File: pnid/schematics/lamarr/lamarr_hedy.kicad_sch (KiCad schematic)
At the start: 98 parts

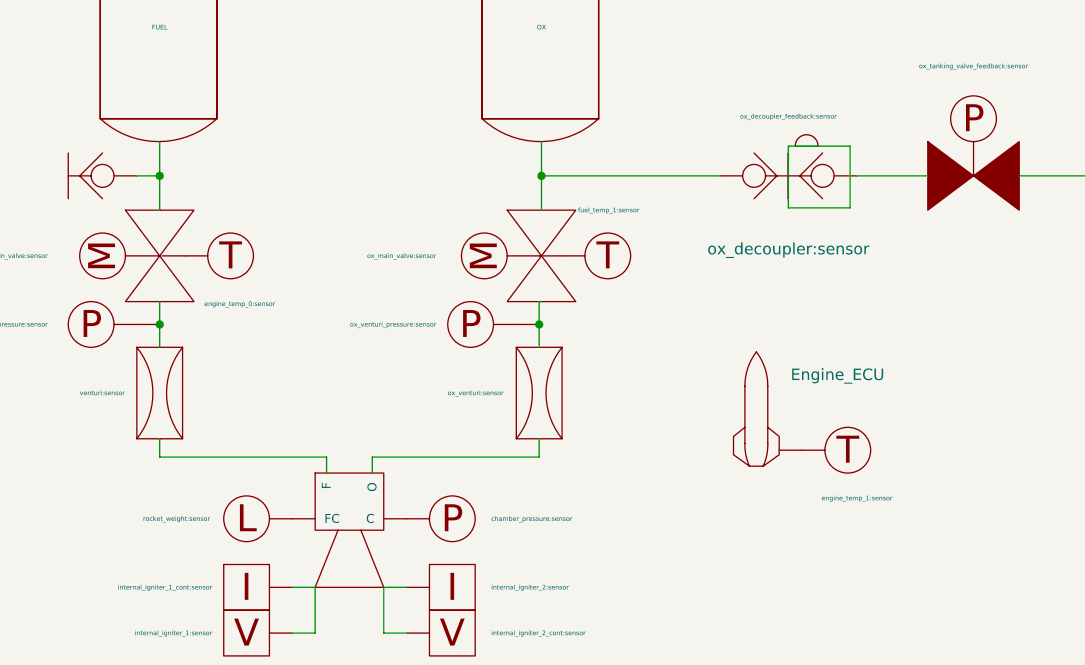
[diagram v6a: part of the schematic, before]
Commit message: Changed Temp Sensor Locations
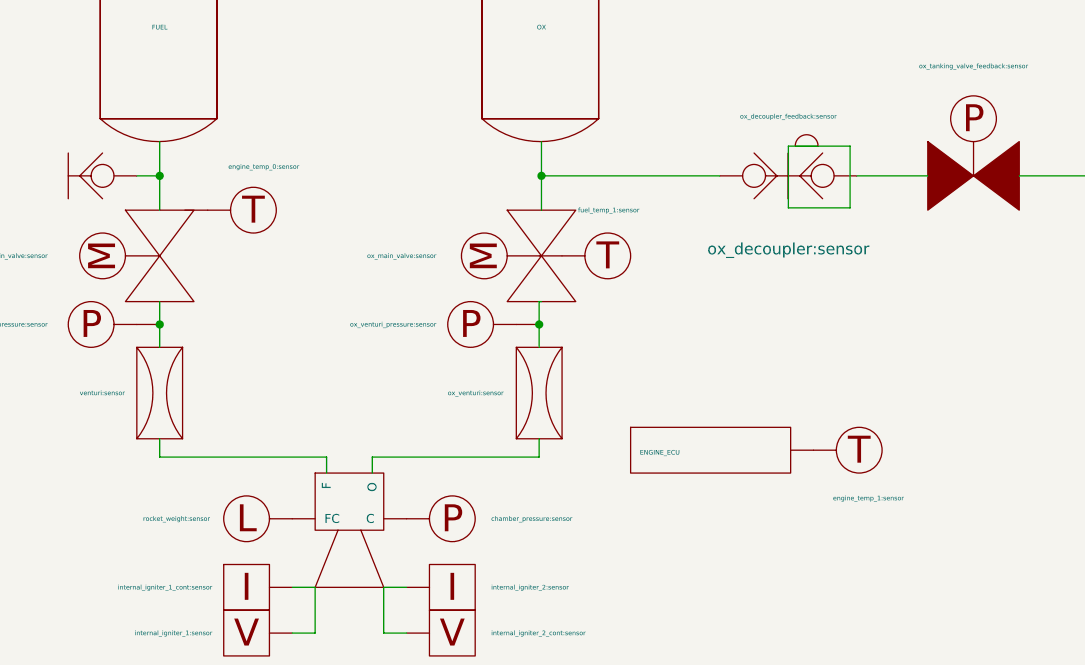
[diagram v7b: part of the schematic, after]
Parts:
- removed Engine_ECU: (no value), symbol PnID:Rocket_Channel
- added engineecu: ENGINE_ECU, symbol PnID:Label
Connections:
- net at engine.~ (O): now also venturi1.~; no longer ox_venturi.~
- net at venturi1.~: now also fuel_main_valve.~, fuel_venturi_pressure.~; no longer engine.~ (O)
- net at dewar_needle_valve?.~: now also C2.~, C3.~; no longer C1.~
- net at Orifice2.~: now also fuel_pressurant_valve.~, pressurantPressureRegulator1.~
- new net: engine.~ (O), ox_venturi.~
- new net: OX.~, ox_main_valve.~, ox_quick_connect.~
- new net: DewarOverPressureValve?.~, LOX.~, dewar_pressurize_solenoid.~
- new net: C1.~, dewar_needle_valve?.~
- new net: Orifice1.~, ox_pressurant_valve.~, pressurantPressureRegulator2.~
- new net: FUEL.~, fuel_main_valve.~, ox_quick_connect1.~
- now unconnected: Orifice1.~
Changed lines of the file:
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@@
 	)
 	(symbol
-		(lib_id "PnID:Rocket_Channel")
-		(at 144.78 175.26 0)
-		(unit 1)
-		(exclude_from_sim no)
-		(in_bom yes)
-		(on_board yes)
-		(dnp no)
-		(fields_autoplaced yes)
-		(property "Reference" "Engine_ECU"
-			(at 148.59 169.4179 0)
-			(effects
-				(font
-					(size 1.27 1.27)
-				)
-				(justify left)
-			)
-		)
-		(property "Value" ""
-			(at 148.59 170.6879 0)
-			(effects
-				(font
-					(size 1.27 1.27)
-				)
-				(justify left)
-			)
-		)
-		(property "Footprint" ""
-			(at 144.78 178.308 0)
-			(effects
-				(font
-					(size 1.27 1.27)
-				)
-				(hide yes)
-			)
-		)
-		(property "Datasheet" ""
-			(at 144.78 178.308 0)
-			(effects
-				(font
-					(size 1.27 1.27)
-				)
-				(hide yes)
-			)
-		)
-		(property "Description" ""
-			(at 144.78 175.26 0)
-			(effects
-				(font
-					(size 1.27 1.27)
-				)
-				(hide yes)
-			)
-		)
-		(property "Unit" " "
-			(at 148.59 171.9579 0)
-			(effects
-				(font
-					(size 1.27 1.27)
-				)
-				(justify left)
-			)
-		)
-		(property "Action_Reference" " "
-			(at 148.59 174.4979 0)
-			(effects
-				(font
-					(size 1.27 1.27)
-				)
-				(justify left)
-			)
-		)
-		(property "Data_Content" " "
-			(at 148.59 177.0379 0)
-			(effects
-				(font
-					(size 1.27 1.27)
-				)
-				(justify left)
-			)
-		)
-		(instances
-			(project ""
-				(path "/604fc9f3-63a6-4133-afd1-4a5c2507dc1d"
-					(reference "Engine_ECU")
-					(unit 1)
-				)
-			)
-		)
-	)
-	(symbol
 		(lib_id "PnID-Lib:PressureRegulator")
 		(at 120.904 66.04 90)
@@
 	(symbol
 		(lib_id "PnID-Lib:Sensor_Temperature")
-		(at 154.94 177.8 0)
+		(at 156.21 177.8 0)
 		(unit 1)
 		(exclude_from_sim no)
@@
 		(dnp no)
 		(property "Reference" "engine_ECU_temperature"
-			(at 158.75 177.165 0)
+			(at 160.02 177.165 0)
 			(effects
 				(font
@@
 		)
 		(property "Value" "engine_temp_1:sensor"
-			(at 152.019 183.134 0)
+			(at 153.289 183.134 0)
 			(effects
 				(font
@@
 		)
 		(property "Footprint" ""
-			(at 154.94 177.8 0)
+			(at 156.21 177.8 0)
 			(effects
 				(font
@@
 		)
 		(property "Datasheet" ""
-			(at 154.94 177.8 0)
+			(at 156.21 177.8 0)
 			(effects
 				(font
@@
 		)
 		(property "Description" ""
-			(at 154.94 177.8 0)
+			(at 156.21 177.8 0)
 			(effects
 				(font
@@
 		)
 		(property "Unit" "˚C"
-			(at 154.94 177.8 0)
+			(at 156.21 177.8 0)
 			(effects
 				(font
@@
 		)
 		(property "Action_Reference" " "
-			(at 154.94 177.8 0)
+			(at 156.21 177.8 0)
 			(effects
 				(font
@@
 	)
 	(symbol
+		(lib_name "Label_4")
+		(lib_id "PnID:Label")
+		(at 138.43 177.8 0)
+		(unit 1)
+		(exclude_from_sim no)
+		(in_bom yes)
+		(on_board yes)
+		(dnp no)
+		(property "Reference" "engineecu"
+			(at 138.43 172.212 0)
+			(effects
+				(font
+					(size 1.27 1.27)
+				)
+				(hide yes)
+			)
+		)
+		(property "Value" "ENGINE_ECU"
+			(at 131.826 178.054 0)
+			(effects
+				(font
+					(size 0.508 0.508)
+				)
+				(justify left)
+			)
+		)
+		(property "Footprint" ""
+			(at 138.43 177.8 0)
+			(effects
+				(font
+					(size 1.27 1.27)
+				)
+				(hide yes)
+			)
+		)
+		(property "Datasheet" ""
+			(at 138.43 177.8 0)
+			(effects
+				(font
+					(size 1.27 1.27)
+				)
+				(hide yes)
+			)
+		)
+		(property "Description" ""
+			(at 138.43 177.8 0)
+			(effects
+				(font
+					(size 1.27 1.27)
+				)
+				(hide yes)
+			)
+		)
+		(instances
+			(project "lamarr_hedy"
+				(path "/604fc9f3-63a6-4133-afd1-4a5c2507dc1d"
+					(reference "engineecu")
+					(unit 1)
+				)
+			)
+		)
+	)
+	(symbol
 		(lib_id "PnID-Lib:Valve_Pneumatic_NO")
 		(at 53.594 34.798 90)
@@
 	)
 	(symbol
+		(lib_name "Sensor_Temperature_1")
 		(lib_id "PnID-Lib:Sensor_Temperature")
-		(at 86.36 156.21 0)
+		(at 88.9 151.13 0)
 		(unit 1)
 		(exclude_from_sim no)
@@
 		(dnp no)
 		(property "Reference" "fuel_main_valve_temperature"
-			(at 90.17 155.575 0)
+			(at 92.71 150.495 0)
 			(effects
 				(font
@@
 		)
 		(property "Value" "engine_temp_0:sensor"
-			(at 83.439 161.544 0)
+			(at 86.106 146.304 0)
 			(effects
 				(font
@@
 		)
 		(property "Footprint" ""
-			(at 86.36 156.21 0)
+			(at 88.9 151.13 0)
 			(effects
 				(font
@@
 		)
 		(property "Datasheet" ""
-			(at 86.36 156.21 0)
+			(at 88.9 151.13 0)
 			(effects
 				(font
@@
 		)
 		(property "Description" ""
-			(at 86.36 156.21 0)
+			(at 88.9 151.13 0)
 			(effects
 				(font
@@
 		)
 		(property "Unit" "˚C"
-			(at 86.36 156.21 0)
+			(at 88.9 151.13 0)
 			(effects
 				(font
@@
 		)
 		(property "Action_Reference" " "
-			(at 86.36 156.21 0)
+			(at 88.9 151.13 0)
 			(effects
 				(font

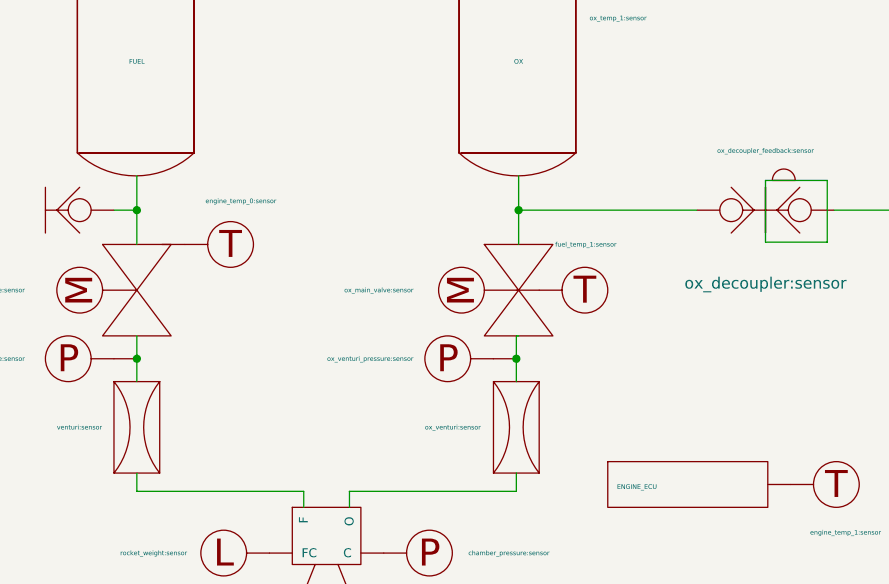
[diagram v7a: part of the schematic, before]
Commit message: minor changes to kvaser install script, added temp Sensors to PnID, archived old PnIDs, modified Clodflow and prepress sequences
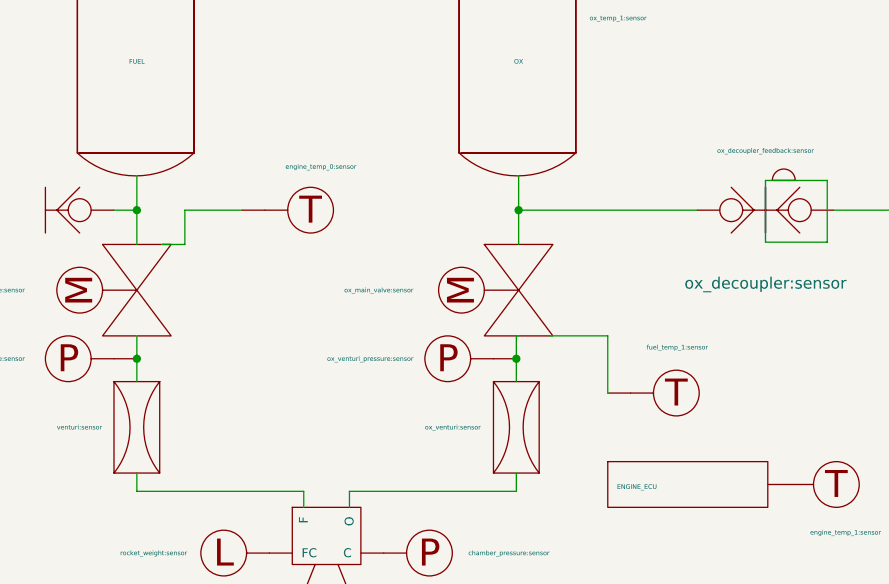
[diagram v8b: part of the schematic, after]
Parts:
- renumbered thrust to rocket_weight
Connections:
- net at engine.~ (O): now also venturi1.~; no longer ox_venturi.~
- net at venturi1.~: now also fuel_main_valve.~, fuel_venturi_pressure.~; no longer engine.~ (O)
- net at dewar_needle_valve?.~: now also C2.~, C3.~; no longer C1.~
- net at Orifice2.~: now also fuel_pressurant_valve.~, pressurantPressureRegulator1.~
- new net: engine.~ (O), ox_venturi.~
- new net: OX.~, ox_main_valve.~, ox_quick_connect.~
- new net: DewarOverPressureValve?.~, LOX.~, dewar_pressurize_solenoid.~
- new net: C1.~, dewar_needle_valve?.~
- new net: Orifice1.~, ox_pressurant_valve.~, pressurantPressureRegulator2.~
- new net: FUEL.~, fuel_main_valve.~, ox_quick_connect1.~
- now unconnected: Orifice1.~
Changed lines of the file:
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@@
 	(wire
 		(pts
+			(xy 124.46 161.29) (xy 130.81 161.29)
+		)
+		(stroke
+			(width 0)
+			(type default)
+		)
+	)
+	(wire
+		(pts
+			(xy 90.17 147.32) (xy 83.82 147.32)
+		)
+		(stroke
+			(width 0)
+			(type default)
+		)
+	)
+	(wire
+		(pts
 			(xy 21.59 56.134) (xy 28.194 56.134)
 		)
@@
 	(wire
 		(pts
+			(xy 130.81 161.29) (xy 130.81 167.64)
+		)
+		(stroke
+			(width 0)
+			(type default)
+		)
+	)
+	(wire
+		(pts
 			(xy 229.87 95.25) (xy 226.568 95.25)
 		)
@@
 	(wire
 		(pts
+			(xy 83.82 147.32) (xy 83.82 151.13)
+		)
+		(stroke
+			(width 0)
+			(type default)
+		)
+	)
+	(wire
+		(pts
 			(xy 216.408 95.25) (xy 216.535 95.25)
 		)
@@
 	(wire
 		(pts
+			(xy 81.28 151.13) (xy 83.82 151.13)
+		)
+		(stroke
+			(width 0)
+			(type default)
+		)
+	)
+	(wire
+		(pts
 			(xy 78.486 45.974) (xy 78.486 49.53)
 		)
@@
 		(on_board yes)
 		(dnp no)
-		(property "Reference" "thrust"
+		(property "Reference" "rocket_weight"
 			(at 90.8812 178.2318 0)
 			(effects
@@
 			(project "lamarr_hedy"
 				(path "/604fc9f3-63a6-4133-afd1-4a5c2507dc1d"
-					(reference "thrust")
+					(reference "rocket_weight")
 					(unit 1)
 				)
@@
 	(symbol
 		(lib_id "PnID-Lib:Sensor_Temperature")
-		(at 128.27 156.21 0)
+		(at 138.43 167.64 0)
 		(unit 1)
 		(exclude_from_sim no)
@@
 		(dnp no)
 		(property "Reference" "ox_main_valve_servo_temperature"
-			(at 132.08 155.575 0)
+			(at 142.24 167.005 0)
 			(effects
 				(font
@@
 		)
 		(property "Value" "fuel_temp_1:sensor"
-			(at 124.968 151.13 0)
+			(at 135.128 162.56 0)
 			(effects
 				(font
@@
 		)
 		(property "Footprint" ""
-			(at 128.27 156.21 0)
+			(at 138.43 167.64 0)
 			(effects
 				(font
@@
 		)
 		(property "Datasheet" ""
-			(at 128.27 156.21 0)
+			(at 138.43 167.64 0)
 			(effects
 				(font
@@
 		)
 		(property "Description" ""
-			(at 128.27 156.21 0)
+			(at 138.43 167.64 0)
 			(effects
 				(font
@@
 		)
 		(property "Unit" "˚C"
-			(at 128.27 156.21 0)
+			(at 138.43 167.64 0)
 			(effects
 				(font
@@
 		)
 		(property "Action_Reference" " "
-			(at 128.27 156.21 0)
+			(at 138.43 167.64 0)
 			(effects
 				(font
@@
 		(lib_name "Sensor_Temperature_1")
 		(lib_id "PnID-Lib:Sensor_Temperature")
-		(at 88.9 151.13 0)
+		(at 97.79 147.32 0)
 		(unit 1)
 		(exclude_from_sim no)
@@
 		(dnp no)
 		(property "Reference" "fuel_main_valve_temperature"
-			(at 92.71 150.495 0)
+			(at 101.6 146.685 0)
 			(effects
 				(font
@@
 		)
 		(property "Value" "engine_temp_0:sensor"
-			(at 86.106 146.304 0)
+			(at 94.996 142.494 0)
 			(effects
 				(font
@@
 		)
 		(property "Footprint" ""
-			(at 88.9 151.13 0)
+			(at 97.79 147.32 0)
 			(effects
 				(font
@@
 		)
 		(property "Datasheet" ""
-			(at 88.9 151.13 0)
+			(at 97.79 147.32 0)
 			(effects
 				(font
@@
 		)
 		(property "Description" ""
-			(at 88.9 151.13 0)
+			(at 97.79 147.32 0)
 			(effects
 				(font
@@
 		)
 		(property "Unit" "˚C"
-			(at 88.9 151.13 0)
+			(at 97.79 147.32 0)
 			(effects
 				(font
@@
 		)
 		(property "Action_Reference" " "
-			(at 88.9 151.13 0)
+			(at 97.79 147.32 0)
 			(effects
 				(font
